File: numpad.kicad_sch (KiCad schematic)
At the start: 53 parts, among them SW2 SW_Push, U1 BlackPill_STLINK, U4 TRRS

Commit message: Manufacturing Prep
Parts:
- added D111, D112, D113: LED, LED_THT:LED_D5.0mm_Clear, symbol Device:LED
- added R1, R2, R3: R, Keebio-Parts:Resistor, symbol Device:R
- SW2: footprint Keebio-Parts:SW_Tactile_SPST_Angled_MJTP1117 -> Button_Switch_SMD:SW_SPST_PTS645Sx43SMTR92
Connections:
- net NGND: now also D111.1 (K), D112.1 (K), D113.1 (K)
- net at U1.2 (PB13): now also R1.1
- net at U1.3 (PB14): now also R2.1
- net at U1.4 (PB15): now also R3.1
- new net: D112.2 (A), R2.2
- new net: D113.2 (A), R3.2
- new net: D111.2 (A), R1.2
- no-connect marks 25 -> 22
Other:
- moved on the sheet: H1, H2, H3, H4

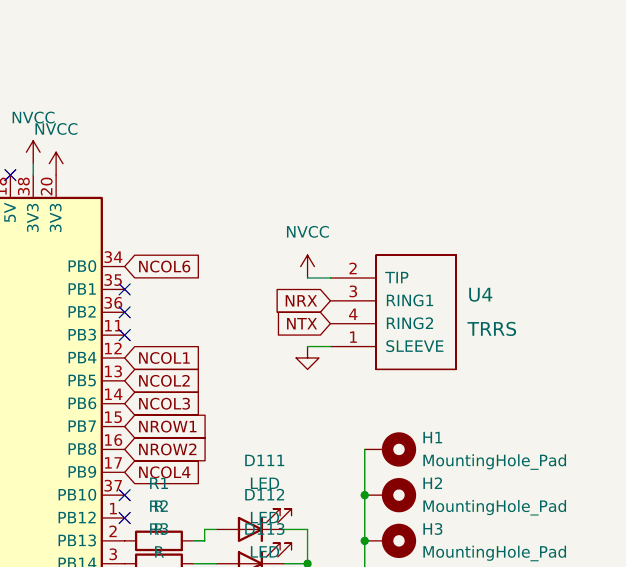
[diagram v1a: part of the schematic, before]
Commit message: Diode and Jack fixes, Silkscreen additons
Diode and TRRS Jack footprints replaced with available parts.
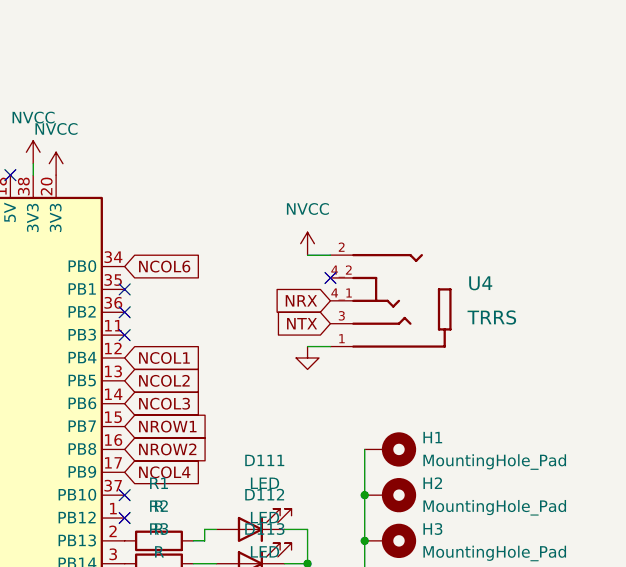
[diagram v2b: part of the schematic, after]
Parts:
- D100, D101, D102, D103, D104, D105, D106, D107, D108, D109, D110, D88, D89, D90, D91, D92, D93, D94, D95, D96, D97, D98, D99: footprint Diode_SMD:D_1210_3225Metric -> Diode_SMD:D_SOD-323_HandSoldering
- U4: footprint Keebio-Parts:TRRS-PJ-320A -> 54_00174:TENSILITY_54-00174; symbol keebio:TRRS -> 54-00174:54-00174; MANUFACTURER (none) -> TENSILITY; MAXIMUM_PACKAGE_HEIGHT (none) -> 6mm; PARTREV (none) -> A; SNAPEDA_PN (none) -> 54-00174; STANDARD (none) -> Manufacturer Recommendations
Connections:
- net NRX: now also U4.4_1; no longer U4.3 (RING1)
- net NTX: now also U4.3; no longer U4.4 (RING2)
- no-connect marks 22 -> 23
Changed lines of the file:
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@@
 	)
 	(no_connect
+		(at 175.26 44.45)
+	)
+	(no_connect
 		(at 127 71.12)
 	)
@@
 	(wire
 		(pts
-			(xy 172.72 44.45) (xy 175.26 44.45)
+			(xy 172.72 41.91) (xy 175.26 41.91)
 		)
 		(stroke
@@
 			)
 		)
-		(property "Footprint" "Diode_SMD:D_1210_3225Metric"
+		(property "Footprint" "Diode_SMD:D_SOD-323_HandSoldering"
 			(at 74.93 92.71 0)
 			(effects
@@
 			)
 		)
-		(property "Footprint" "Diode_SMD:D_1210_3225Metric"
+		(property "Footprint" "Diode_SMD:D_SOD-323_HandSoldering"
 			(at 24.13 50.8 0)
 			(effects
@@
 			)
 		)
-		(property "Footprint" "Diode_SMD:D_1210_3225Metric"
+		(property "Footprint" "Diode_SMD:D_SOD-323_HandSoldering"
 			(at 62.23 36.83 0)
 			(effects
@@
 	)
 	(symbol
-		(lib_id "keebio:TRRS")
-		(at 184.15 54.61 0)
+		(lib_id "54-00174:54-00174")
+		(at 182.88 46.99 180)
 		(unit 1)
 		(exclude_from_sim no)
@@
 		(fields_autoplaced yes)
 		(property "Reference" "U4"
-			(at 190.5 46.355 0)
+			(at 190.5 45.085 0)
 			(effects
 				(font
 					(size 1.524 1.524)
 				)
-				(justify left)
+				(justify right)
 			)
 		)
 		(property "Value" "TRRS"
-			(at 190.5 50.165 0)
+			(at 190.5 48.895 0)
 			(effects
 				(font
 					(size 1.524 1.524)
 				)
-				(justify left)
+				(justify right)
 			)
 		)
-		(property "Footprint" "Keebio-Parts:TRRS-PJ-320A"
-			(at 187.96 54.61 0)
+		(property "Footprint" "54_00174:TENSILITY_54-00174"
+			(at 182.88 46.99 0)
 			(effects
 				(font
-					(size 1.524 1.524)
+					(size 1.27 1.27)
 				)
+				(justify left bottom)
 				(hide yes)
 			)
 		)
 		(property "Datasheet" ""
-			(at 187.96 54.61 0)
+			(at 182.88 46.99 0)
 			(effects
 				(font
-					(size 1.524 1.524)
+					(size 1.27 1.27)
 				)
+				(justify left bottom)
 				(hide yes)
 			)
 		)
 		(property "Description" ""
-			(at 184.15 54.61 0)
+			(at 182.88 46.99 0)
+			(effects
+				(font
+					(size 1.27 1.27)
+				)
+				(hide yes)
+			)
+		)
+		(property "PARTREV" "A"
+			(at 182.88 46.99 0)
+			(effects
+				(font
+					(size 1.27 1.27)
+				)
+				(justify left bottom)
+				(hide yes)
+			)
+		)
+		(property "STANDARD" "Manufacturer Recommendations"
+			(at 182.88 46.99 0)
+			(effects
+				(font
+					(size 1.27 1.27)
+				)
+				(justify left bottom)
+				(hide yes)
+			)
+		)
+		(property "SNAPEDA_PN" "54-00174"
+			(at 182.88 46.99 0)
 			(effects
 				(font
 					(size 1.27 1.27)
 				)
+				(justify left bottom)
+				(hide yes)
+			)
+		)
+		(property "MAXIMUM_PACKAGE_HEIGHT" "6mm"
+			(at 182.88 46.99 0)
+			(effects
+				(font
+					(size 1.27 1.27)
+				)
+				(justify left bottom)
+				(hide yes)
+			)
+		)
+		(property "MANUFACTURER" "TENSILITY"
+			(at 182.88 46.99 0)
+			(effects
+				(font
+					(size 1.27 1.27)
+				)
+				(justify left bottom)
 				(hide yes)
 			)
@@
 		(pin "2"
 		)
-		(pin "4"
+		(pin "4_1"
 		)
 		(pin "3"
@@
 		(pin "1"
 		)
+		(pin "4_2"
+		)
 		(instances
 			(project "theBoerd"
@@
 			)
 		)
-		(property "Footprint" "Diode_SMD:D_1210_3225Metric"
+		(property "Footprint" "Diode_SMD:D_SOD-323_HandSoldering"
 			(at 87.63 64.77 0)
 			(effects
@@
 			)
 		)
-		(property "Footprint" "Diode_SMD:D_1210_3225Metric"
+		(property "Footprint" "Diode_SMD:D_SOD-323_HandSoldering"
 			(at 49.53 36.83 0)
 			(effects
@@
 			)
 		)
-		(property "Footprint" "Diode_SMD:D_1210_3225Metric"
+		(property "Footprint" "Diode_SMD:D_SOD-323_HandSoldering"
 			(at 62.23 50.8 0)
 			(effects
@@
 			)
 		)
-		(property "Footprint" "Diode_SMD:D_1210_3225Metric"
+		(property "Footprint" "Diode_SMD:D_SOD-323_HandSoldering"
 			(at 49.53 92.71 0)
 			(effects
@@
 			)
 		)
-		(property "Footprint" "Diode_SMD:D_1210_3225Metric"
+		(property "Footprint" "Diode_SMD:D_SOD-323_HandSoldering"
 			(at 74.93 78.74 0)
 			(effects
@@
 			)
 		)
-		(property "Footprint" "Diode_SMD:D_1210_3225Metric"
+		(property "Footprint" "Diode_SMD:D_SOD-323_HandSoldering"
 			(at 62.23 78.74 0)
 			(effects
@@
 			)
 		)
-		(property "Footprint" "Diode_SMD:D_1210_3225Metric"
+		(property "Footprint" "Diode_SMD:D_SOD-323_HandSoldering"
 			(at 36.83 78.74 0)
 			(effects
@@
 			)
 		)
-		(property "Footprint" "Diode_SMD:D_1210_3225Metric"
+		(property "Footprint" "Diode_SMD:D_SOD-323_HandSoldering"
 			(at 36.83 36.83 0)
 			(effects
@@
 	(symbol
 		(lib_id "power:VCC")
-		(at 172.72 44.45 0)
+		(at 172.72 41.91 0)
 		(unit 1)
 		(exclude_from_sim no)
@@
 		(fields_autoplaced yes)
 		(property "Reference" "#PWR015"
-			(at 172.72 48.26 0)
+			(at 172.72 45.72 0)
 			(effects
 				(font
@@
 		)
 		(property "Value" "NVCC"
-			(at 172.72 39.37 0)
+			(at 172.72 36.83 0)
 			(effects
 				(font
@@
 		)
 		(property "Footprint" ""
-			(at 172.72 44.45 0)
+			(at 172.72 41.91 0)
 			(effects
 				(font
@@
 		)
 		(property "Datasheet" ""
-			(at 172.72 44.45 0)
+			(at 172.72 41.91 0)
 			(effects
 				(font
@@
 		)
 		(property "Description" "Power symbol creates a global label with name \"VCC\""
-			(at 172.72 44.45 0)
+			(at 172.72 41.91 0)
 			(effects
 				(font
@@
 			)
 		)
-		(property "Footprint" "Diode_SMD:D_1210_3225Metric"
+		(property "Footprint" "Diode_SMD:D_SOD-323_HandSoldering"
 			(at 87.63 78.74 0)
 			(effects
@@
 			)
 		)
-		(property "Footprint" "Diode_SMD:D_1210_3225Metric"
+		(property "Footprint" "Diode_SMD:D_SOD-323_HandSoldering"
 			(at 74.93 64.77 0)
 			(effects
@@
 			)
 		)
-		(property "Footprint" "Diode_SMD:D_1210_3225Metric"
+		(property "Footprint" "Diode_SMD:D_SOD-323_HandSoldering"
 			(at 36.83 64.77 0)
 			(effects
@@
 			)
 		)
-		(property "Footprint" "Diode_SMD:D_1210_3225Metric"
+		(property "Footprint" "Diode_SMD:D_SOD-323_HandSoldering"
 			(at 49.53 64.77 0)
 			(effects
@@
 			)
 		)
-		(property "Footprint" "Diode_SMD:D_1210_3225Metric"
+		(property "Footprint" "Diode_SMD:D_SOD-323_HandSoldering"
 			(at 49.53 78.74 0)
 			(effects
@@
 			)
 		)
-		(property "Footprint" "Diode_SMD:D_1210_3225Metric"
+		(property "Footprint" "Diode_SMD:D_SOD-323_HandSoldering"
 			(at 49.53 50.8 0)
 			(effects
@@
 			)
 		)
-		(property "Footprint" "Diode_SMD:D_1210_3225Metric"
+		(property "Footprint" "Diode_SMD:D_SOD-323_HandSoldering"
 			(at 87.63 92.71 0)
 			(effects
@@
 			)
 		)
-		(property "Footprint" "Diode_SMD:D_1210_3225Metric"
+		(property "Footprint" "Diode_SMD:D_SOD-323_HandSoldering"
 			(at 24.13 92.71 0)
 			(effects
@@
 			)
 		)
-		(property "Footprint" "Diode_SMD:D_1210_3225Metric"
+		(property "Footprint" "Diode_SMD:D_SOD-323_HandSoldering"
 			(at 36.83 50.8 0)
 			(effects
@@
 			)
 		)
-		(property "Footprint" "Diode_SMD:D_1210_3225Metric"
+		(property "Footprint" "Diode_SMD:D_SOD-323_HandSoldering"
 			(at 24.13 78.74 0)
 			(effects
@@
 			)
 		)
-		(property "Footprint" "Diode_SMD:D_1210_3225Metric"
+		(property "Footprint" "Diode_SMD:D_SOD-323_HandSoldering"
 			(at 24.13 36.83 0)
 			(effects
@@
 			)
 		)
-		(property "Footprint" "Diode_SMD:D_1210_3225Metric"
+		(property "Footprint" "Diode_SMD:D_SOD-323_HandSoldering"
 			(at 24.13 64.77 0)
 			(effects

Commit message: Key Labeling
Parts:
- renumbered CH110 to CH16, CH107 to CHF13, CH106 to CHF14, CH104 to CHF15, CH109 to CHF17, CH108 to CHF18, CH103 to CHKP0, CH99 to CHKP1, CH100 to CHKP2, CH101 to CHKP3, CH96 to CHKP4, CH97 to CHKP5, CH98 to CHKP6, CH92 to CHKP7, CH93 to CHKP8, CH94 to CHKP9, CH90 to CHKPAST1, CH105 to CHKPDOT1, CH102 to CHKPENT1, CH91 to CHKPMNS1, CH95 to CHKPPLS1, CH89 to CHKPSLSH1, CH88 to CHNUMLCK1
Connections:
- net at R3.1: now also D113.2 (A); no longer U1.4 (PB15)
- net at R3.2: now also U1.4 (PB15); no longer D113.2 (A)
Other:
- moved on the sheet: D111, D112, D113, H1, H2, H3, H4, R2, R3

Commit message: PDF Exports
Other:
- moved on the sheet: D111, D112, D113, H1, H2, H3, H4, R1, R2, R3, SW2, U1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
